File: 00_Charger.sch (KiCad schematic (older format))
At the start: 56 parts, among them J303 TB001-500-02BE CUI_Devices, J401 TB001-500-02BE CUI_Devices, Q303 2N7002, Q304 2N7002, Q305 FDD4685-F085, Q306 2N7002, Q307 BSS84, Q308 2N7002, Q309 FDD4685-F085, U401 MAX1873TEEE

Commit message: vor änderungen von der Arbeit
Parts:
- U401: symbol Battery_Management:MAX1873TEEE -> MukkeBox-rescue:MAX1873TEEE-Battery_Management
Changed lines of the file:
@@
 $EndDescr
 $Comp
-L Battery_Management:MAX1873TEEE U401
+L MukkeBox-rescue:MAX1873TEEE-Battery_Management U401
 U 1 1 5E73C573
 P 6400 3800

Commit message: Charger austauschen gegen bq24610
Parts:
- removed D401, D402: STPS1045B-TR, Package_TO_SOT_SMD:TO-252-2, symbol Device:D_Schottky_x2_KCom_AKA
- removed Q305: FDD4685-F085, Package_TO_SOT_SMD:TO-252-2, symbol Device:Q_NMOS_GSD
- added C302: 47n, Capacitor_SMD:C_0603_1608Metric_Pad1.05x0.95mm_HandSolder, symbol Device:C_Small
- added C? (x3): 100n, Capacitor_SMD:C_0603_1608Metric_Pad1.05x0.95mm_HandSolder, symbol Device:C_Small
- added Q301: 2N7002, Package_TO_SOT_SMD:SOT-23, symbol Transistor_FET:2N7002
- added Q305: FDD5614P, Package_TO_SOT_SMD:TO-252-2, symbol Device:Q_PMOS_GDS
- added Q? (x2): HSBB3103, Package_SON:Diodes_PowerDI3333-8, symbol MySymbols:HSBB3103
- added R301, R302: 1M, Resistor_SMD:R_0603_1608Metric_Pad1.05x0.95mm_HandSolder, symbol Device:R_Small
- added R303: DNP, Resistor_SMD:R_0603_1608Metric_Pad1.05x0.95mm_HandSolder, symbol Device:R_Small
- added R?: 100K, Resistor_SMD:R_0603_1608Metric_Pad1.05x0.95mm_HandSolder, symbol Device:R_Small
- added R?: 1K, Resistor_SMD:R_0603_1608Metric_Pad1.05x0.95mm_HandSolder, symbol Device:R_Small
- added RAC: 33m, Resistor_SMD:R_1206_3216Metric_Pad1.42x1.75mm_HandSolder, symbol Device:R_Small
- added U301, U302: STPS30M60DJF, Package_TO_SOT_SMD:TDSON-8-1_HandSoldering, symbol MukkeBox-rescue:Diode-TDSON-8-MySymbols
- added U?: BQ24610, Package_DFN_QFN:VQFN-24-1EP_4x4mm_P0.5mm_EP2.45x2.45mm_ThermalVias, symbol MySymbols:BQ24610
- C402, C403: value 100n -> 220n; footprint Capacitor_SMD:C_0603_1608Metric_Pad1.05x0.95mm_HandSolder -> Capacitor_SMD:C_1210_3225Metric
- C404: value 220n -> 2.2u 30V; footprint Capacitor_SMD:C_0603_1608Metric_Pad1.05x0.95mm_HandSolder -> Capacitor_SMD:C_1210_3225Metric
- C405, C406: value 100n -> 10n
- L302: value 22uH 6100-220K-RC -> 10u Würth 7443251000; footprint Inductor_THT:L_Radial_D12.0mm_P6.00mm_MuRATA_1900R -> Inductor_SMD:L_Wuerth_HCI-1050
- Q309: value FDD4685-F085 -> FDD5614P
- R307: value 1M -> 100K
- R310: value 1K -> 100K
- R402, R403: value 4.7k 1% -> 100K
- R_CSB401: value 200m -> 68m
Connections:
- wire segments 159 -> 198
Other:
- note added: "9uA"
- note added: "tau=0,047s"
- moved on the sheet: C301, C309, C412, F301, J303, J401, Q303, Q306, Q307, Q308, R307, R310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

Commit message: Charger ausgetauscht, Mosfet und Dioden durch billigere ersetzt
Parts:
- removed C301, C410: 100n, Capacitor_SMD:C_0603_1608Metric_Pad1.05x0.95mm_HandSolder, symbol Device:C_Small
- removed C304: 68u, Capacitor_THT:CP_Radial_D5.0mm_P2.50mm, symbol Device:CP1_Small
- removed C401: 1u, Capacitor_SMD:C_0603_1608Metric_Pad1.05x0.95mm_HandSolder, symbol Device:C_Small
- removed C402, C403: 220n, Capacitor_SMD:C_1210_3225Metric, symbol Device:C_Small
- removed C404: 2.2u 30V, Capacitor_SMD:C_1210_3225Metric, symbol Device:C_Small
- removed C405, C406: 10n, Capacitor_SMD:C_0603_1608Metric_Pad1.05x0.95mm_HandSolder, symbol Device:C_Small
- removed C407, C408: 47n, Capacitor_SMD:C_0603_1608Metric_Pad1.05x0.95mm_HandSolder, symbol Device:C_Small
- removed C409: 1n, Capacitor_SMD:C_0603_1608Metric_Pad1.05x0.95mm_HandSolder, symbol Device:C_Small
- removed Q304: 2N7002, Package_TO_SOT_SMD:SOT-23, symbol Transistor_FET:2N7002
- removed Q305, Q309: FDD5614P, Package_TO_SOT_SMD:TO-252-2, symbol Device:Q_PMOS_GDS
- removed R401: 100k, Resistor_SMD:R_0603_1608Metric_Pad1.05x0.95mm_HandSolder, symbol Device:R_Small
- removed R402, R403: 100K, Resistor_SMD:R_0603_1608Metric_Pad1.05x0.95mm_HandSolder, symbol Device:R_Small
- removed R404: 10k, Resistor_SMD:R_0603_1608Metric_Pad1.05x0.95mm_HandSolder, symbol Device:R_Small
- removed R405, R406: 4.7k, Resistor_SMD:R_0603_1608Metric_Pad1.05x0.95mm_HandSolder, symbol Device:R_Small
- removed R407, R408, R409, R410: 1K, Resistor_SMD:R_0603_1608Metric_Pad1.05x0.95mm_HandSolder, symbol Device:R_Small
- removed R_CSS401: 33m, Resistor_SMD:R_1206_3216Metric_Pad1.42x1.75mm_HandSolder, symbol Device:R_Small
- removed U301, U302: STPS30M60DJF, Package_TO_SOT_SMD:TDSON-8-1_HandSoldering, symbol MukkeBox-rescue:Diode-TDSON-8-MySymbols
- removed U401: MAX1873TEEE, Package_SO:QSOP-16_3.9x4.9mm_P0.635mm, symbol MukkeBox-rescue:MAX1873TEEE-Battery_Management
- added C15C301, C305, C312, C313: 100n, Capacitor_SMD:C_0603_1608Metric_Pad1.05x0.95mm_HandSolder, symbol Device:C_Small
- added C304, C307, C310: 1u, Capacitor_SMD:C_1210_3225Metric, symbol Device:C_Small
- added C308, C311: 33n, Capacitor_SMD:C_0603_1608Metric_Pad1.05x0.95mm_HandSolder, symbol Device:C_Small
- added C314: 22p, Capacitor_SMD:C_0603_1608Metric_Pad1.05x0.95mm_HandSolder, symbol Device:C_Small
- added D301: BAT54C, Package_TO_SOT_SMD:SOT-23, symbol Diode:BAT54C
- added Q305, Q309: VS6412AE, Package_SON:Diodes_PowerDI3333-8, symbol Transistor_FET:CSD18504Q5A
- added Q310, Q311: HSBB3103, Package_SON:Diodes_PowerDI3333-8, symbol MukkeBox-rescue:HSBB3103-MySymbols
- added R15C301, R19C301, R1C301, R304, R3C301, R5C301, R7C301: 100K, Resistor_SMD:R_0603_1608Metric_Pad1.05x0.95mm_HandSolder, symbol Device:R_Small
- added R2C301: 700K, Resistor_SMD:R_0603_1608Metric_Pad1.05x0.95mm_HandSolder, symbol Device:R_Small
- added R308: 10R, Resistor_SMD:R_0603_1608Metric_Pad1.05x0.95mm_HandSolder, symbol Device:R_Small
- added R4C301: 22K, Resistor_SMD:R_0603_1608Metric_Pad1.05x0.95mm_HandSolder, symbol Device:R_Small
- added R6C301, R8C301: 10K, Resistor_SMD:R_0603_1608Metric_Pad1.05x0.95mm_HandSolder, symbol Device:R_Small
- added R9C301: 2K2, Resistor_SMD:R_0603_1608Metric_Pad1.05x0.95mm_HandSolder, symbol Device:R_Small
- added R9C302: 6K8, Resistor_SMD:R_0603_1608Metric_Pad1.05x0.95mm_HandSolder, symbol Device:R_Small
- C302: value 47n -> 100n
- C411: value 68u -> 10u
- Q302, Q304: renamed from Q?; symbol MySymbols:HSBB3103 -> MukkeBox-rescue:HSBB3103-MySymbols
- R301, R302: value 1M -> 100K
- R303: value DNP -> 100K
- R306: renamed from R?; value 1K -> 100K
- RAC301: renamed from RAC; value 33m -> 10m
- RSR301: renamed from R_CSB401; value 68m -> 10m
- U301: renamed from U?; symbol MySymbols:BQ24610 -> MukkeBox-rescue:BQ24610-MySymbols
- gave numbers to parts that had none: 4
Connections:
- net labels added: +3.3V, CE, CHARGER_PG, CHARGER_STAT1, CHARGER_STAT2, SRN, SRP, VREF
- net labels removed: CHARGER_IOUT, IOUT, POWER_SUPPLY
- wire segments 198 -> 210
- no-connect marks 0 -> 1
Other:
- note added: "0.3A Precharge"
- note added: "1.5A Quickcharge"
- note added: "16.8V Setpoint"
- note added: "3A AC-Adapter"
- note added: "6.16hr Fastcharge Timer"
- note added: "Resonsnzfrequenz: 15,92kHz"
- note added: "V_bat=(1+R2/R1)*2.1V"
- note removed: "3,06V @ 3A Chargecurrent"
- note removed: "4,08V @ 3A Chargecurrent"
- note removed: "9uA"
- note removed: "I=1mA"
- note removed: "IOUT=20(R_SCB*I_CHG) = \n20*0,068*3A= 4,08V"
- note removed: "R_CSB - Charge Current Limit\n68m: Icharge = 0.2V/R_CSB = 3A\nfür 2 Zellen Parallel = 0.5Charging Rate\n"
- note removed: "R_CSS - Input Current Limit\n33m: Iin = 0.1V/RCSS = 3A"
- note removed: "Spannung 20V in Ladekabel"
- note removed: "T Version des IC für 4 Li-Ion Zellen"
- note removed: "U VADJ: 4.2V +/- 5.25%"
- note removed: "Zum Lition-Zellen-Block"
- note removed: "ca. 4-5V"
- note removed: "tau=0,047s"
- moved on the sheet: C301, C302, C303, C306, C309, C411, C412, F301, J303, J401, L302, Q301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

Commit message: Änderungen Arbeit hinzugefügt: Layout neuer Charger
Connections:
- net GND: now also U301.17 (GND)
- net at U301.22 (BTST): now also D301.3
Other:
- moved on the sheet: D301, R308
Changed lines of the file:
@@
 EESchema Schematic File Version 4
-LIBS:MukkeBox-cache
-EELAYER 26 0
+EELAYER 30 0
 EELAYER END
 $Descr A4 11693 8268
@@
 L Device:R_Small R308
 U 1 1 5ED8FE46
-P 6600 1400
-F 0 "R308" H 6450 1350 50  0000 C CNN
-F 1 "10R" H 6450 1450 50  0000 C CNN
-F 2 "Resistor_SMD:R_0603_1608Metric_Pad1.05x0.95mm_HandSolder" H 6600 1400 50  0001 C CNN
-F 3 "~" H 6600 1400 50  0001 C CNN
-	1    6600 1400
+P 6800 1400
+F 0 "R308" H 6950 1350 50  0000 C CNN
+F 1 "10R" H 6950 1450 50  0000 C CNN
+F 2 "Resistor_SMD:R_0603_1608Metric_Pad1.05x0.95mm_HandSolder" H 6800 1400 50  0001 C CNN
+F 3 "~" H 6800 1400 50  0001 C CNN
+	1    6800 1400
 	-1   0    0    1
 $EndComp
@@
 	4550 1100 4550 800
 Wire Wire Line
-	4550 800  6600 800
-Wire Wire Line
-	6600 800  6600 1300
-Wire Wire Line
-	6600 1500 6600 1600
-Wire Wire Line
-	6600 1600 6500 1600
+	4550 800  6800 800
+Wire Wire Line
+	6800 800  6800 1300
+Wire Wire Line
+	6800 1500 6800 1600
+Wire Wire Line
+	6800 1600 6500 1600
 $Comp
 L Device:C_Small C310
@@
 $EndComp
 Wire Wire Line
-	6850 1600 6600 1600
-Connection ~ 6600 1600
+	6850 1600 6800 1600
+Connection ~ 6800 1600
 $Comp
 L power:GND #PWR0315
@@
 $EndComp
 Wire Wire Line
-	6500 2500 7450 2500
+	6500 2500 6900 2500
 Wire Wire Line
 	6500 2200 7150 2200
@@
 Wire Wire Line
 	6500 2950 6700 2950
-Wire Wire Line
-	6900 2750 6500 2750
 $Comp
 L Diode:BAT54C D301
 U 1 1 5F7968FE
-P 7100 2850
-F 0 "D301" V 7054 2937 50  0000 L CNN
-F 1 "BAT54C" V 7145 2937 50  0000 L CNN
-F 2 "Package_TO_SOT_SMD:SOT-23" H 7175 2975 50  0001 L CNN
-F 3 "http://www.diodes.com/_files/datasheets/ds11005.pdf" H 7020 2850 50  0001 C CNN
-	1    7100 2850
-	0    1    1    0
-$EndComp
-Wire Wire Line
-	6900 2850 6900 2750
-Wire Wire Line
-	6700 2950 6900 2950
-Wire Wire Line
-	6900 2950 6900 3150
-Wire Wire Line
-	6900 3150 7100 3150
+P 7000 2650
+F 0 "D301" H 7150 2550 50  0000 L CNN
+F 1 "BAT54C" H 7100 2450 50  0000 L CNN
+F 2 "Package_TO_SOT_SMD:SOT-23" H 7075 2775 50  0001 L CNN
+F 3 "http://www.diodes.com/_files/datasheets/ds11005.pdf" H 6920 2650 50  0001 C CNN
+	1    7000 2650
+	1    0    0    -1
+$EndComp
 Connection ~ 6700 2950
-NoConn ~ 7100 2550
+Wire Wire Line
+	6500 2850 6600 2850
+NoConn ~ 6700 2650
+Wire Wire Line
+	7300 2650 7400 2650
+Wire Wire Line
+	7400 2650 7400 2950
+Wire Wire Line
+	6700 2950 7400 2950
+$Comp
+L power:PWR_FLAG #FLG0106
+U 1 1 5EE0E3DC
+P 6500 1400
+F 0 "#FLG0106" H 6500 1475 50  0001 C CNN
+F 1 "PWR_FLAG" H 6500 1573 50  0000 C CNN
+F 2 "" H 6500 1400 50  0001 C CNN
+F 3 "~" H 6500 1400 50  0001 C CNN
+	1    6500 1400
+	1    0    0    -1
+$EndComp
+Wire Wire Line
+	6500 1400 6500 1600
+Connection ~ 6500 1600
+$Comp
+L power:GND #PWR0130
+U 1 1 5EE44E7E
+P 6700 3600
+F 0 "#PWR0130" H 6700 3350 50  0001 C CNN
+F 1 "GND" H 6600 3500 50  0000 C CNN
+F 2 "" H 6700 3600 50  0001 C CNN
+F 3 "" H 6700 3600 50  0001 C CNN
+	1    6700 3600
+	1    0    0    -1
+$EndComp
+Wire Wire Line
+	6700 3600 6700 3500
+Wire Wire Line
+	6700 3500 6500 3500
+$Comp
+L power:PWR_FLAG #FLG0115
+U 1 1 5EE52A50
+P 6900 2500
+F 0 "#FLG0115" H 6900 2575 50  0001 C CNN
+F 1 "PWR_FLAG" H 6900 2673 50  0000 C CNN
+F 2 "" H 6900 2500 50  0001 C CNN
+F 3 "~" H 6900 2500 50  0001 C CNN
+	1    6900 2500
+	1    0    0    -1
+$EndComp
+Connection ~ 6900 2500
+Wire Wire Line
+	6900 2500 7450 2500
+$Comp
+L power:PWR_FLAG #FLG0116
+U 1 1 5EE52FF2
+P 6600 2850
+F 0 "#FLG0116" H 6600 2925 50  0001 C CNN
+F 1 "PWR_FLAG" H 6800 2900 50  0000 C CNN
+F 2 "" H 6600 2850 50  0001 C CNN
+F 3 "~" H 6600 2850 50  0001 C CNN
+	1    6600 2850
+	1    0    0    -1
+$EndComp
+Connection ~ 6600 2850
+Wire Wire Line
+	6600 2850 7000 2850
 $EndSCHEMATC

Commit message: Layout fertig, Schaltplan erneut checken
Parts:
- removed J303: TB001-500-02BE CUI_Devices, TerminalBlock_RND:TerminalBlock_RND_205-00045_1x02_P5.00mm_Horizontal, symbol Connector:Screw_Terminal_01x02
- added J303: TB001-500-04BE CUI_Devices, TerminalBlock_RND:TerminalBlock_RND_205-00047_1x04_P5.00mm_Horizontal, symbol Connector:Screw_Terminal_01x04
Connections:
- net GND: now also U301.25 (GND), J303.1 (Pin_1), J303.3 (Pin_3)
- net at F301.1: now also J303.4 (Pin_4)
- net TS: now reaches C305.2, R9C301.1, R9C302.2, U301.6 (TS)
- net TS: now also J303.2 (Pin_2)
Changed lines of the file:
@@
 EESchema Schematic File Version 4
-EELAYER 30 0
+LIBS:MukkeBox-cache
+EELAYER 26 0
 EELAYER END
 $Descr A4 11693 8268
@@
 PACK+
 $Comp
-L Connector:Screw_Terminal_01x02 J303
-U 1 1 5ED37ADF
-P 1150 6300
-F 0 "J303" H 1150 6050 50  0000 C CNN
-F 1 "TB001-500-02BE CUI_Devices" V 1300 6500 50  0000 C CNN
-F 2 "TerminalBlock_RND:TerminalBlock_RND_205-00045_1x02_P5.00mm_Horizontal" H 1150 6300 50  0001 C CNN
-F 3 "https://www.mouser.de/datasheet/2/670/tb001-500-1550615.pdf" H 1150 6300 50  0001 C CNN
-	1    1150 6300
-	-1   0    0    1
-$EndComp
-$Comp
 L power:GND #PWR0301
 U 1 1 5ED37D03
-P 1350 6400
-F 0 "#PWR0301" H 1350 6150 50  0001 C CNN
-F 1 "GND" H 1500 6300 50  0000 C CNN
-F 2 "" H 1350 6400 50  0001 C CNN
-F 3 "" H 1350 6400 50  0001 C CNN
-	1    1350 6400
-	1    0    0    -1
-$EndComp
-Wire Wire Line
-	1350 6300 1350 6400
+P 1350 6800
+F 0 "#PWR0301" H 1350 6550 50  0001 C CNN
+F 1 "GND" H 1500 6700 50  0000 C CNN
+F 2 "" H 1350 6800 50  0001 C CNN
+F 3 "" H 1350 6800 50  0001 C CNN
+	1    1350 6800
+	1    0    0    -1
+$EndComp
 Wire Wire Line
 	10650 1100 10500 1100
@@
 Wire Wire Line
 	6600 2850 7000 2850
+$Comp
+L power:GND #PWR0131
+U 1 1 5EDA6D9E
+P 6100 4700
+F 0 "#PWR0131" H 6100 4450 50  0001 C CNN
+F 1 "GND" H 6105 4527 50  0000 C CNN
+F 2 "" H 6100 4700 50  0001 C CNN
+F 3 "" H 6100 4700 50  0001 C CNN
+	1    6100 4700
+	1    0    0    -1
+$EndComp
+Wire Wire Line
+	6100 4700 6100 4400
+$Comp
+L Connector:Screw_Terminal_01x04 J?
+U 1 1 5EDE91C5
+P 1000 6400
+AR Path="/5E751A81/5EDE91C5" Ref="J?"  Part="1"
+AR Path="/5E73BB4A/5EDE91C5" Ref="J303"  Part="1"
+F 0 "J303" H 900 5900 50  0000 L CNN
+F 1 "TB001-500-04BE CUI_Devices" V 1150 5900 50  0000 L CNN
+F 2 "TerminalBlock_RND:TerminalBlock_RND_205-00047_1x04_P5.00mm_Horizontal" H 1000 6400 50  0001 C CNN
+F 3 "~" H 1000 6400 50  0001 C CNN
+	1    1000 6400
+	-1   0    0    1
+$EndComp
+Wire Wire Line
+	1350 6800 1350 6500
+Wire Wire Line
+	1350 6500 1200 6500
+Wire Wire Line
+	1200 6300 1350 6300
+Wire Wire Line
+	1350 6300 1350 6500
+Connection ~ 1350 6500
+Wire Wire Line
+	1350 6200 1200 6200
+Text Label 4150 4400 2    50   ~ 0
+TS
+Wire Wire Line
+	4550 4400 4150 4400
+Text Label 1200 6400 0    50   ~ 0
+TS
 $EndSCHEMATC

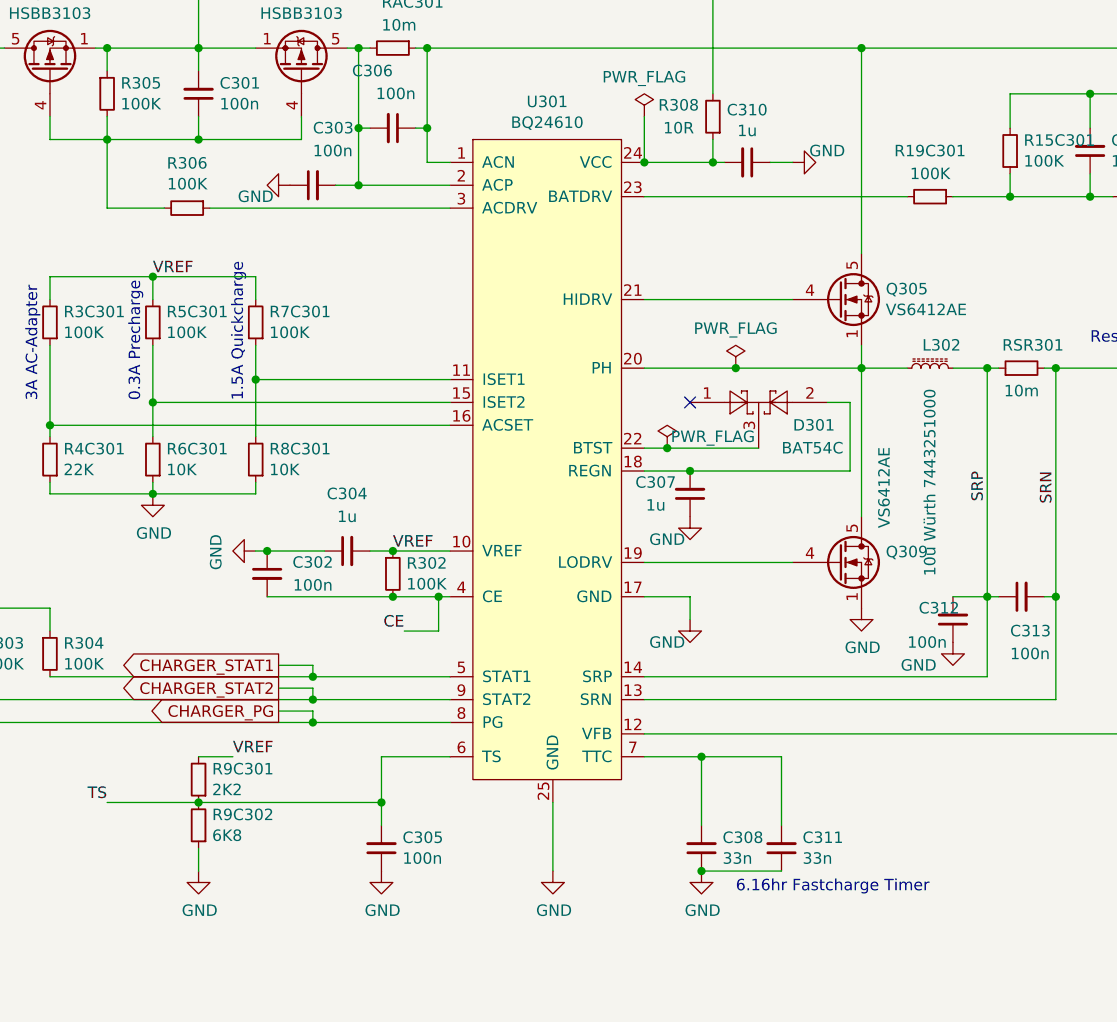
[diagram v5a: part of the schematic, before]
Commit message: Änderungen von der Arbeit, Viele LCSC Teile für teurere ausgetauscht
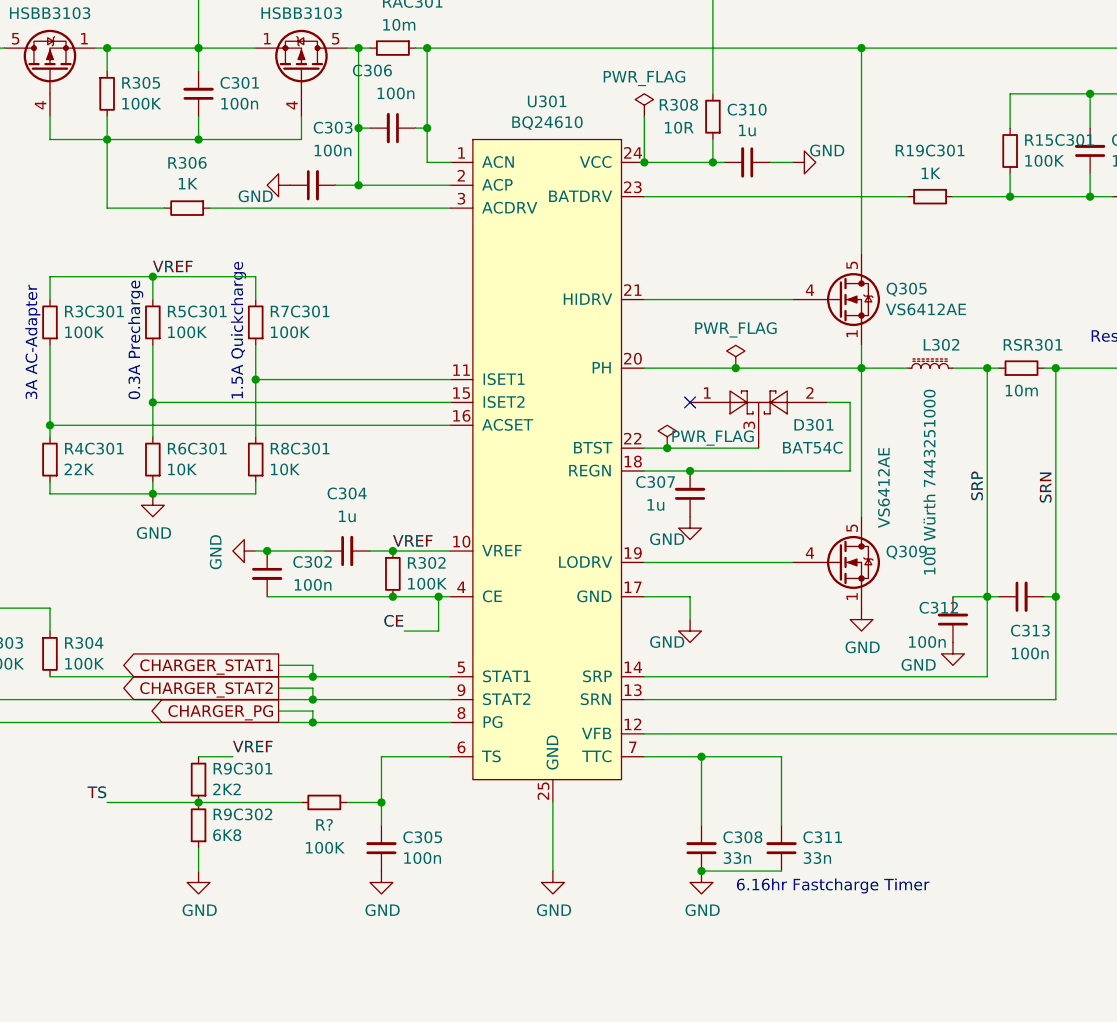
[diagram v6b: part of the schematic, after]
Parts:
- added R?: 100K, Resistor_SMD:R_0603_1608Metric_Pad1.05x0.95mm_HandSolder, symbol Device:R_Small
- R19C301, R306: value 100K -> 1K
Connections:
- net TS: now also R?.2; no longer C305.2, U301.6 (TS)
- new net: C305.2, R?.1, U301.6 (TS)
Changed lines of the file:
@@
 P 4500 1800
 F 0 "R306" V 4304 1800 50  0000 C CNN
-F 1 "100K" V 4395 1800 50  0000 C CNN
+F 1 "1K" V 4395 1800 50  0000 C CNN
 F 2 "Resistor_SMD:R_0603_1608Metric_Pad1.05x0.95mm_HandSolder" H 4500 1800 50  0001 C CNN
 F 3 "~" H 4500 1800 50  0001 C CNN
@@
 P 7750 1750
 F 0 "R19C301" V 7550 1750 50  0000 C CNN
-F 1 "100K" V 7650 1750 50  0000 C CNN
+F 1 "1K" V 7650 1750 50  0000 C CNN
 F 2 "Resistor_SMD:R_0603_1608Metric_Pad1.05x0.95mm_HandSolder" H 7750 1750 50  0001 C CNN
 F 3 "~" H 7750 1750 50  0001 C CNN
@@
 	3150 4050 3150 3850
 Wire Wire Line
-	5350 4200 5350 4400
-Wire Wire Line
-	4550 4400 5350 4400
-Connection ~ 5350 4400
-Wire Wire Line
-	5350 4400 5350 4500
-Wire Wire Line
 	6750 4200 6750 4500
 Wire Wire Line
@@
 Text Label 1200 6400 0    50   ~ 0
 TS
+$Comp
+L Device:R_Small R?
+U 1 1 5EDD4FC6
+P 5100 4400
+F 0 "R?" V 5200 4400 50  0000 C CNN
+F 1 "100K" V 5300 4400 50  0000 C CNN
+F 2 "Resistor_SMD:R_0603_1608Metric_Pad1.05x0.95mm_HandSolder" H 5100 4400 50  0001 C CNN
+F 3 "~" H 5100 4400 50  0001 C CNN
+	1    5100 4400
+	0    1    1    0
+$EndComp
+Wire Wire Line
+	5350 4200 5350 4400
+Wire Wire Line
+	5200 4400 5350 4400
+Connection ~ 5350 4400
+Wire Wire Line
+	5350 4400 5350 4500
+Wire Wire Line
+	5000 4400 4550 4400
 $EndSCHEMATC

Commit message: Fast fertig TODO: Connector umverdrahten mit beschriftung
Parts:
- C411: footprint Capacitor_THT:CP_Radial_D6.3mm_P2.50mm -> Capacitor_THT:CP_Radial_D4.0mm_P2.00mm
- gave numbers to parts that had none: 1
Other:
- moved on the sheet: C309, F301, J303, Q301, Q307, Q308, R313, R314, R315, R316, R317, R318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

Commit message: Bestellung abgeschickt
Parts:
- R313: value 470K -> 100K
- R314: value 47K -> 10K
- R413: value 47K -> 100K
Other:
- note added: "50ms Charge Time"
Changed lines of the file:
@@
 P 2100 2000
 F 0 "R413" H 2159 2046 50  0000 L CNN
-F 1 "47K" H 2159 1955 50  0000 L CNN
+F 1 "100K" H 2159 1955 50  0000 L CNN
 F 2 "Resistor_SMD:R_0603_1608Metric_Pad1.05x0.95mm_HandSolder" H 2100 2000 50  0001 C CNN
 F 3 "~" H 2100 2000 50  0001 C CNN
@@
 P 2500 6650
 F 0 "R313" H 2800 6600 50  0000 R CNN
-F 1 "470K" H 2800 6700 50  0000 R CNN
+F 1 "100K" H 2800 6700 50  0000 R CNN
 F 2 "Resistor_SMD:R_0603_1608Metric_Pad1.05x0.95mm_HandSolder" H 2500 6650 50  0001 C CNN
 F 3 "~" H 2500 6650 50  0001 C CNN
@@
 P 2500 6950
 F 0 "R314" H 2800 6900 50  0000 R CNN
-F 1 "47K" H 2800 7000 50  0000 R CNN
+F 1 "10K" H 2800 7000 50  0000 R CNN
 F 2 "Resistor_SMD:R_0603_1608Metric_Pad1.05x0.95mm_HandSolder" H 2500 6950 50  0001 C CNN
 F 3 "~" H 2500 6950 50  0001 C CNN
@@
 Wire Wire Line
 	5000 4400 4550 4400
+Text Notes 1400 6750 0    50   ~ 0
+50ms Charge Time
 $EndSCHEMATC
